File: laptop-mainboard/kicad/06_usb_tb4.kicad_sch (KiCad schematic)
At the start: 13 parts, among them U23 JHL8540_TB4, U28 HD3SS3220_Mux, U29 HD3SS3220_Mux, U30 SY6280_5V_SW, U31 SY6280_5V_SW, U32 SY6280_5V_SW, U33 SY6280_5V_SW

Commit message: Rev B: echte AM5-Pinbelegung, Kleinteile, EliteBook-850-G7-Format
- AM5-Pinmap (1718 Pins, WikiChip/Wikimedia Public Domain) als CSV,
  Sockel-Footprint mit echten Padnamen und 1708 Signal-Netzen im Board
- Blatt 10: MLCC-Baenke, 11 ESD-Arrays, USB2-Chokes, Straps; 48-MHz-Quarz;
  beidseitige Bestueckung (B.Cu) mit Kollisionspruefung pro Seite
- Board 340x112mm im EliteBook-850-G7-Layout: USB-C-100W-PD an der
  Barrel-Jack-Position, TB4/HDMI/USB-A/RJ45 rechts, USB-A/Klinke links,
  HP-Akku 3S/56Wh, HP-FPC-Steckplaetze (Pinouts zu verifizieren)
- GND-Stitching-Vias, MDI-/DP-Korridore, 645 Board-Netze
- Renderer tools/render_board.py erzeugt docs/board_render.png
- Doku: elitebook.md neu, grenzen.md/README/power/layout aktualisiert

Co-Authored-By: Claude Fable 5 <noreply@anthropic.com>
Claude-Session: https://claude.ai/code/session_01E8mU1RUAv938Hs69waADCc
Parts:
- removed J_USBC2: USB-C_10G, laptop_mainboard:USBC_24, symbol lm:USB-C_10G_J_USBC2
- removed J_USBC3: USB-C_10G, laptop_mainboard:USBC_24, symbol lm:USB-C_10G_J_USBC3
- removed U28: HD3SS3220_Mux, laptop_mainboard:QFN30_4x4, symbol lm:HD3SS3220_Mux_U28
- removed U29: HD3SS3220_Mux, laptop_mainboard:QFN30_4x4, symbol lm:HD3SS3220_Mux_U29
- removed U30: SY6280_5V_SW, laptop_mainboard:SOT23-5, symbol lm:SY6280_5V_SW_U30
- removed U31: SY6280_5V_SW, laptop_mainboard:SOT23-5, symbol lm:SY6280_5V_SW_U31
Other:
- note added: "Barrel-Jacks (rechts hinten) = 100W-PD-Ladeport, TB1 = originaler"
- note added: "ESD-Schutz und USB2-Chokes: Blatt 10 (Kleinteile)."
- note added: "Portlayout wie HP EliteBook 850 G7: TB0 sitzt an der Position des"
- note added: "USB-C/TB-Port. Beide Thunderbolt 4 ueber JHL8540."
- note removed: "ESD-Schutz (TPD4E02B04 an allen SS-Paaren, TPD6E05U06 an USB2/CC)"
- note removed: "TB0 = Ladeport (100W Sink via TPS65988, Blatt 1), TB1 = 15W Source."
- note removed: "USB-C Gen2-Ports: Orientierungs-Mux HD3SS3220 pro Port."
- note removed: "direkt an den Buchsen - in Stueckliste, hier nicht gezeichnet."

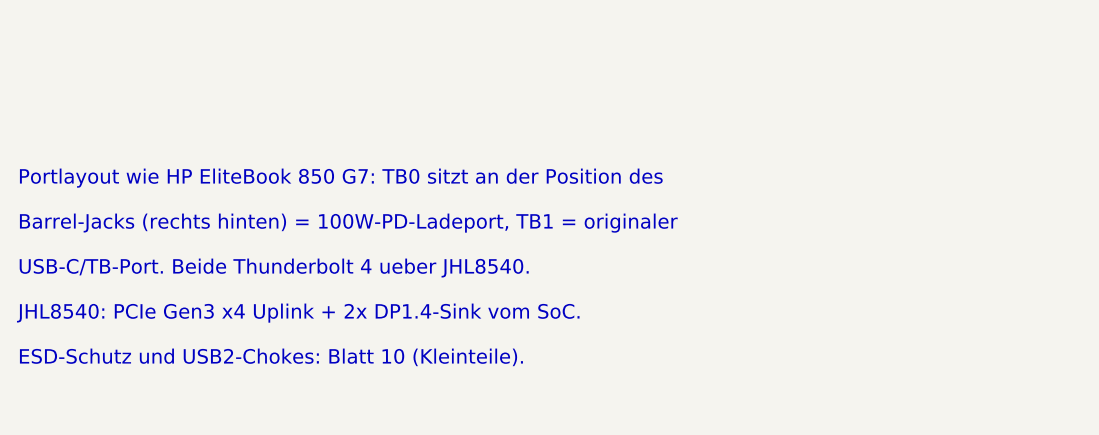
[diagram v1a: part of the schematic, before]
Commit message: Portlayout nach Fotos des Originalgeraets korrigiert
- Rechte Kante hinten->vorn: USB-C-Ladeport 100W (Barrel-Position,
  eigener TPS65987D + Config-Flash, neues Blatt 07_ladeport), USB-A,
  HDMI, 2x USB-C Thunderbolt 4 nebeneinander (JHL8540)
- Kein RJ45 (Original hat keines): Ethernet entfernt, G0/G1 Reserve
- TPS65988 nur noch Source fuer die TB-Ports; breite VBUS_IN-Trasse
  vom Ladeport zum BQ25731
- Interne Anschlusspositionen des Original-Mainboards (Nutzerfoto)
  als Referenztabelle in docs/elitebook.md dokumentiert
- Doku, Blockdiagramm, BOM und Rendering aktualisiert

Co-Authored-By: Claude Fable 5 <noreply@anthropic.com>
Claude-Session: https://claude.ai/code/session_01E8mU1RUAv938Hs69waADCc
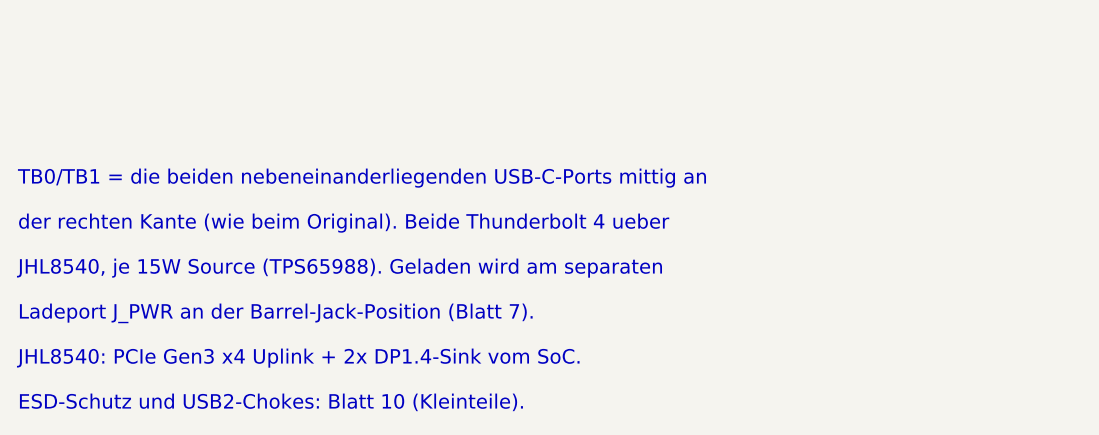
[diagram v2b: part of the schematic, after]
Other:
- note added: "JHL8540, je 15W Source (TPS65988). Geladen wird am separaten"
- note added: "Ladeport J_PWR an der Barrel-Jack-Position (Blatt 7)."
- note added: "TB0/TB1 = die beiden nebeneinanderliegenden USB-C-Ports mittig an"
- note added: "der rechten Kante (wie beim Original). Beide Thunderbolt 4 ueber"
- note removed: "Barrel-Jacks (rechts hinten) = 100W-PD-Ladeport, TB1 = originaler"
- note removed: "Portlayout wie HP EliteBook 850 G7: TB0 sitzt an der Position des"
- note removed: "USB-C/TB-Port. Beide Thunderbolt 4 ueber JHL8540."
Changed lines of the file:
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@@
     (company "Laptop-Mainboard-Projekt")
   )
-  (text "Portlayout wie HP EliteBook 850 G7: TB0 sitzt an der Position des" (exclude_from_sim no) (at 20 260 0)
+  (text "TB0/TB1 = die beiden nebeneinanderliegenden USB-C-Ports mittig an" (exclude_from_sim no) (at 20 260 0)
     (effects (font (size 1.6 1.6)) (justify left))
   )
-  (text "Barrel-Jacks (rechts hinten) = 100W-PD-Ladeport, TB1 = originaler" (exclude_from_sim no) (at 20 265 0)
+  (text "der rechten Kante (wie beim Original). Beide Thunderbolt 4 ueber" (exclude_from_sim no) (at 20 265 0)
     (effects (font (size 1.6 1.6)) (justify left))
   )
-  (text "USB-C/TB-Port. Beide Thunderbolt 4 ueber JHL8540." (exclude_from_sim no) (at 20 270 0)
+  (text "JHL8540, je 15W Source (TPS65988). Geladen wird am separaten" (exclude_from_sim no) (at 20 270 0)
     (effects (font (size 1.6 1.6)) (justify left))
   )
-  (text "JHL8540: PCIe Gen3 x4 Uplink + 2x DP1.4-Sink vom SoC." (exclude_from_sim no) (at 20 275 0)
+  (text "Ladeport J_PWR an der Barrel-Jack-Position (Blatt 7)." (exclude_from_sim no) (at 20 275 0)
     (effects (font (size 1.6 1.6)) (justify left))
   )
-  (text "ESD-Schutz und USB2-Chokes: Blatt 10 (Kleinteile)." (exclude_from_sim no) (at 20 280 0)
+  (text "JHL8540: PCIe Gen3 x4 Uplink + 2x DP1.4-Sink vom SoC." (exclude_from_sim no) (at 20 280 0)
+    (effects (font (size 1.6 1.6)) (justify left))
+  )
+  (text "ESD-Schutz und USB2-Chokes: Blatt 10 (Kleinteile)." (exclude_from_sim no) (at 20 285 0)
     (effects (font (size 1.6 1.6)) (justify left))
   )
@@
     (pin "44")
     (pin "45")
-    (instances (project "laptop-mainboard" (path "/d22f2c28-8e23-5b8e-ba77-63ae2c13187c/57e32864-bd60-524b-a7bf-d320ef10be09" (reference "U23") (unit 1))))
+    (instances (project "laptop-mainboard" (path "/d22f2c28-8e23-5b8e-ba77-63ae2c13187c/ac83ec61-c362-53db-bb4b-0eecc5621248" (reference "U23") (unit 1))))
   )
   (wire (pts (xy 73.33 46.99) (xy 65.71 46.99)) (stroke (width 0) (type default)))
@@
     (pin "16")
     (pin "17")
-    (instances (project "laptop-mainboard" (path "/d22f2c28-8e23-5b8e-ba77-63ae2c13187c/57e32864-bd60-524b-a7bf-d320ef10be09" (reference "J_TB0") (unit 1))))
+    (instances (project "laptop-mainboard" (path "/d22f2c28-8e23-5b8e-ba77-63ae2c13187c/ac83ec61-c362-53db-bb4b-0eecc5621248" (reference "J_TB0") (unit 1))))
   )
   (wire (pts (xy 240.95 46.99) (xy 233.33 46.99)) (stroke (width 0) (type default)))
@@
     (pin "16")
     (pin "17")
-    (instances (project "laptop-mainboard" (path "/d22f2c28-8e23-5b8e-ba77-63ae2c13187c/57e32864-bd60-524b-a7bf-d320ef10be09" (reference "J_TB1") (unit 1))))
+    (instances (project "laptop-mainboard" (path "/d22f2c28-8e23-5b8e-ba77-63ae2c13187c/ac83ec61-c362-53db-bb4b-0eecc5621248" (reference "J_TB1") (unit 1))))
   )
   (wire (pts (xy 240.95 105.41) (xy 233.33 105.41)) (stroke (width 0) (type default)))
@@
     (pin "8")
     (pin "9")
-    (instances (project "laptop-mainboard" (path "/d22f2c28-8e23-5b8e-ba77-63ae2c13187c/57e32864-bd60-524b-a7bf-d320ef10be09" (reference "J_USBA1") (unit 1))))
+    (instances (project "laptop-mainboard" (path "/d22f2c28-8e23-5b8e-ba77-63ae2c13187c/ac83ec61-c362-53db-bb4b-0eecc5621248" (reference "J_USBA1") (unit 1))))
   )
   (wire (pts (xy 402.22 46.99) (xy 394.6 46.99)) (stroke (width 0) (type default)))
@@
     (pin "8")
     (pin "9")
-    (instances (project "laptop-mainboard" (path "/d22f2c28-8e23-5b8e-ba77-63ae2c13187c/57e32864-bd60-524b-a7bf-d320ef10be09" (reference "J_USBA2") (unit 1))))
+    (instances (project "laptop-mainboard" (path "/d22f2c28-8e23-5b8e-ba77-63ae2c13187c/ac83ec61-c362-53db-bb4b-0eecc5621248" (reference "J_USBA2") (unit 1))))
   )
   (wire (pts (xy 402.22 85.09) (xy 394.6 85.09)) (stroke (width 0) (type default)))
@@
     (pin "3")
     (pin "4")
-    (instances (project "laptop-mainboard" (path "/d22f2c28-8e23-5b8e-ba77-63ae2c13187c/57e32864-bd60-524b-a7bf-d320ef10be09" (reference "U32") (unit 1))))
+    (instances (project "laptop-mainboard" (path "/d22f2c28-8e23-5b8e-ba77-63ae2c13187c/ac83ec61-c362-53db-bb4b-0eecc5621248" (reference "U32") (unit 1))))
   )
   (wire (pts (xy 406.03 123.19) (xy 398.41 123.19)) (stroke (width 0) (type default)))
@@
     (pin "3")
     (pin "4")
-    (instances (project "laptop-mainboard" (path "/d22f2c28-8e23-5b8e-ba77-63ae2c13187c/57e32864-bd60-524b-a7bf-d320ef10be09" (reference "U33") (unit 1))))
+    (instances (project "laptop-mainboard" (path "/d22f2c28-8e23-5b8e-ba77-63ae2c13187c/ac83ec61-c362-53db-bb4b-0eecc5621248" (reference "U33") (unit 1))))
   )
   (wire (pts (xy 406.03 146.05) (xy 398.41 146.05)) (stroke (width 0) (type default)))
